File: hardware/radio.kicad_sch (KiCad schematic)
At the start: 5 parts

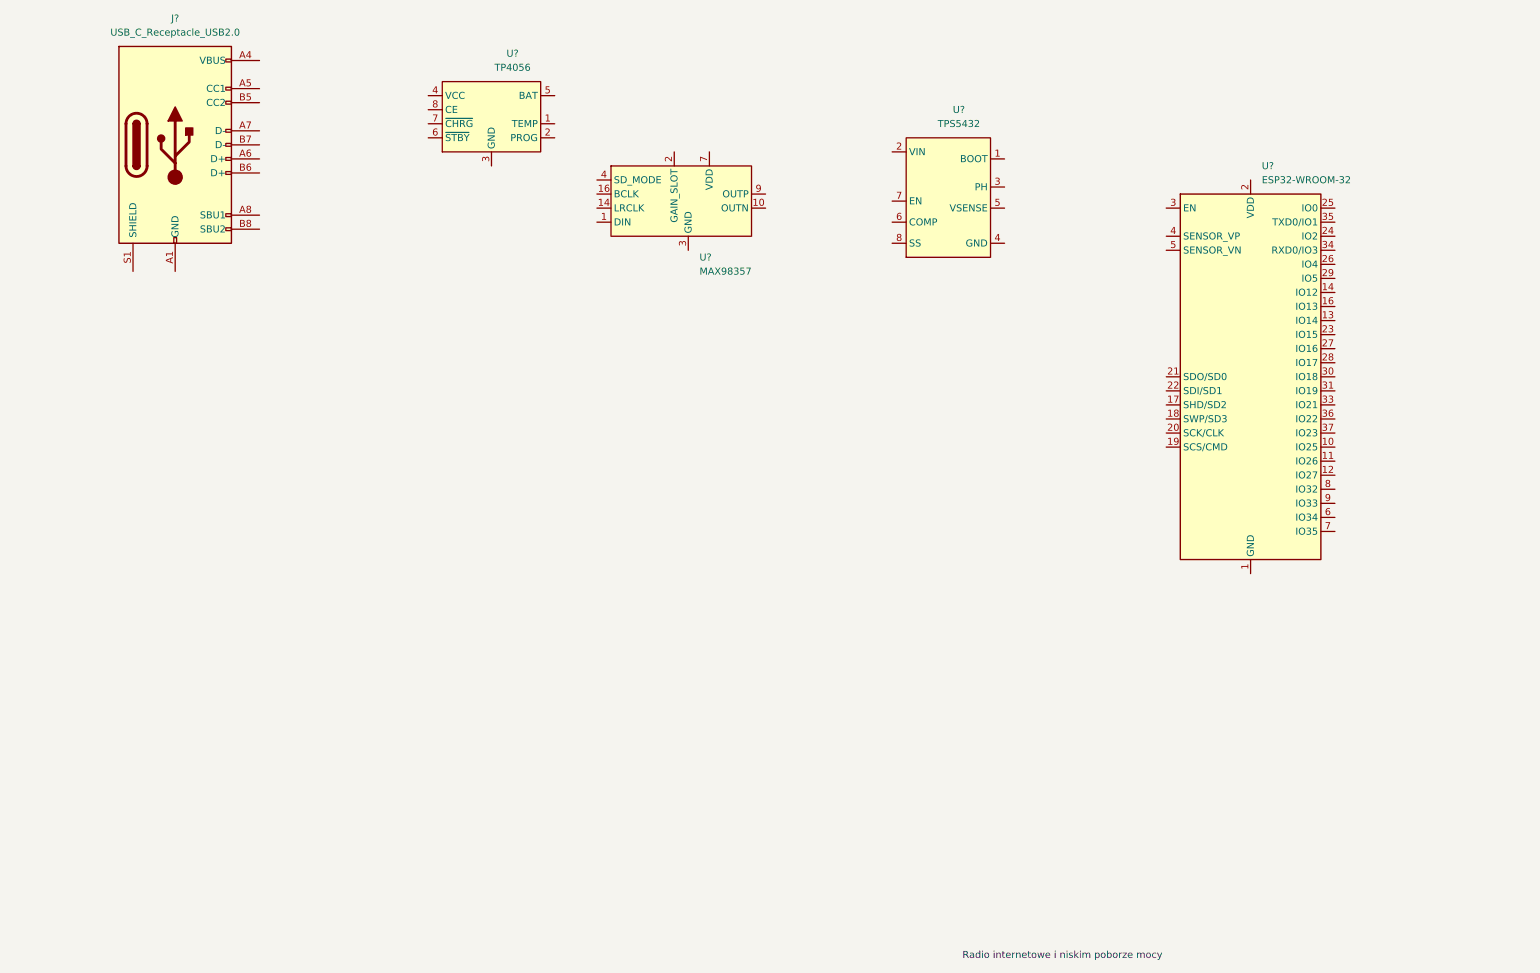
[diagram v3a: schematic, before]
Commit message: aktualizacja opisu symbolu OLED
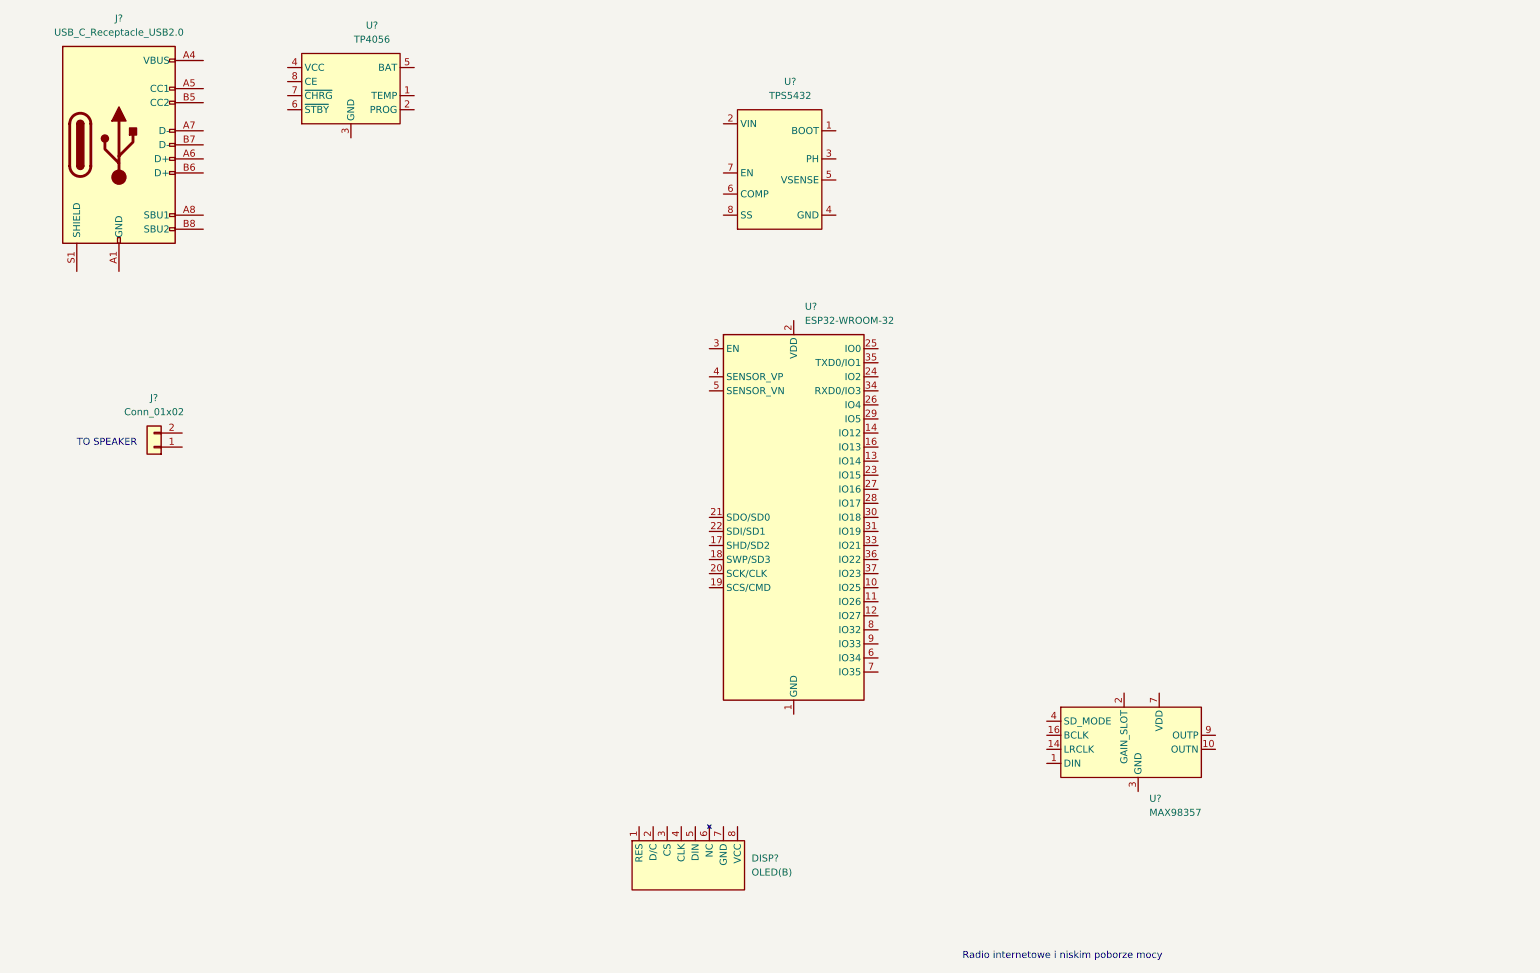
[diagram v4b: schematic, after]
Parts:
- added DISP?: OLED(B), symbol wyswietlacze:OLED(B)
- added J?: Conn_01x02, symbol Connector_Generic:Conn_01x02
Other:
- note added: "TO SPEAKER"
- moved on the sheet: J?, U?
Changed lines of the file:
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@@
     (effects (font (size 1.27 1.27)) (justify left bottom))
   )
-  (symbol (lib_id "scalaki:MAX98357") (at 138.43 53.34 0) (unit 1)
+  (text "TO SPEAKER\n" (at 27.94 97.79 0)
+    (effects (font (size 1.27 1.27)) (justify left bottom))
+  )
+  (symbol (lib_id "Connector_Generic:Conn_01x02") (at 41.91 97.79 180) (unit 1)
+    (in_bom no) (on_board yes) (fields_autoplaced)
+    (property "Reference" "J?" (id 0) (at 41.91 88.9 0))
+    (property "Value" "Conn_01x02" (id 1) (at 41.91 91.44 0))
+    (property "Footprint" "" (id 2) (at 41.91 97.79 0)
+      (effects (font (size 1.27 1.27)) hide)
+    )
+    (property "Datasheet" "~" (id 3) (at 41.91 97.79 0)
+      (effects (font (size 1.27 1.27)) hide)
+    )
+    (pin "1")
+    (pin "2")
+  )
+  (symbol (lib_id "scalaki:MAX98357") (at 219.71 151.13 0) (unit 1)
     (in_bom yes) (on_board yes) (fields_autoplaced)
-    (property "Reference" "U?" (id 0) (at 140.4494 63.5 0)
+    (property "Reference" "U?" (id 0) (at 221.7294 161.29 0)
       (effects (font (size 1.27 1.27)) (justify left))
     )
-    (property "Value" "MAX98357" (id 1) (at 140.4494 66.04 0)
+    (property "Value" "MAX98357" (id 1) (at 221.7294 163.83 0)
       (effects (font (size 1.27 1.27)) (justify left))
     )
-    (property "Footprint" "Package_DFN_QFN:TQFN-16-1EP_3x3mm_P0.5mm_EP1.23x1.23mm" (id 2) (at 138.43 53.34 0)
+    (property "Footprint" "Package_DFN_QFN:TQFN-16-1EP_3x3mm_P0.5mm_EP1.23x1.23mm" (id 2) (at 219.71 151.13 0)
       (effects (font (size 1.27 1.27)) hide)
     )
-    (property "Datasheet" "" (id 3) (at 138.43 53.34 0)
+    (property "Datasheet" "" (id 3) (at 219.71 151.13 0)
       (effects (font (size 1.27 1.27)) hide)
     )
@@
     (pin "9")
   )
-  (symbol (lib_id "RF_Module:ESP32-WROOM-32") (at 240.03 85.09 0) (unit 1)
+  (symbol (lib_id "RF_Module:ESP32-WROOM-32") (at 157.48 110.49 0) (unit 1)
     (in_bom yes) (on_board yes) (fields_autoplaced)
-    (property "Reference" "U?" (id 0) (at 242.0494 46.99 0)
+    (property "Reference" "U?" (id 0) (at 159.4994 72.39 0)
       (effects (font (size 1.27 1.27)) (justify left))
     )
-    (property "Value" "ESP32-WROOM-32" (id 1) (at 242.0494 49.53 0)
+    (property "Value" "ESP32-WROOM-32" (id 1) (at 159.4994 74.93 0)
       (effects (font (size 1.27 1.27)) (justify left))
     )
-    (property "Footprint" "RF_Module:ESP32-WROOM-32" (id 2) (at 240.03 123.19 0)
+    (property "Footprint" "RF_Module:ESP32-WROOM-32" (id 2) (at 157.48 148.59 0)
       (effects (font (size 1.27 1.27)) hide)
     )
-    (property "Datasheet" "https://www.espressif.com/sites/default/files/documentation/esp32-wroom-32_datasheet_en.pdf" (id 3) (at 232.41 83.82 0)
+    (property "Datasheet" "https://www.espressif.com/sites/default/files/documentation/esp32-wroom-32_datasheet_en.pdf" (id 3) (at 149.86 109.22 0)
       (effects (font (size 1.27 1.27)) hide)
     )
@@
     (pin "9")
   )
-  (symbol (lib_id "Connector:USB_C_Receptacle_USB2.0") (at 45.72 43.18 0) (unit 1)
+  (symbol (lib_id "Connector:USB_C_Receptacle_USB2.0") (at 35.56 43.18 0) (unit 1)
     (in_bom yes) (on_board yes) (fields_autoplaced)
-    (property "Reference" "J?" (id 0) (at 45.72 20.32 0))
-    (property "Value" "USB_C_Receptacle_USB2.0" (id 1) (at 45.72 22.86 0))
-    (property "Footprint" "" (id 2) (at 49.53 43.18 0)
+    (property "Reference" "J?" (id 0) (at 35.56 20.32 0))
+    (property "Value" "USB_C_Receptacle_USB2.0" (id 1) (at 35.56 22.86 0))
+    (property "Footprint" "" (id 2) (at 39.37 43.18 0)
       (effects (font (size 1.27 1.27)) hide)
     )
-    (property "Datasheet" "https://www.usb.org/sites/default/files/documents/usb_type-c.zip" (id 3) (at 49.53 43.18 0)
+    (property "Datasheet" "https://www.usb.org/sites/default/files/documents/usb_type-c.zip" (id 3) (at 39.37 43.18 0)
       (effects (font (size 1.27 1.27)) hide)
     )
@@
     (pin "S1")
   )
-  (symbol (lib_id "scalaki:TP4056") (at 102.87 38.1 0) (unit 1)
+  (symbol (lib_id "wyswietlacze:OLED(B)") (at 138.43 173.99 0) (unit 1)
     (in_bom yes) (on_board yes) (fields_autoplaced)
-    (property "Reference" "U?" (id 0) (at 106.68 26.67 0))
-    (property "Value" "TP4056" (id 1) (at 106.68 29.21 0))
-    (property "Footprint" "" (id 2) (at 100.33 39.37 0)
+    (property "Reference" "DISP?" (id 0) (at 149.86 172.0849 0)
+      (effects (font (size 1.27 1.27)) (justify left))
+    )
+    (property "Value" "OLED(B)" (id 1) (at 149.86 174.6249 0)
+      (effects (font (size 1.27 1.27)) (justify left))
+    )
+    (property "Footprint" "" (id 2) (at 146.05 179.07 0)
       (effects (font (size 1.27 1.27)) hide)
     )
-    (property "Datasheet" "" (id 3) (at 100.33 39.37 0)
+    (property "Datasheet" "" (id 3) (at 146.05 179.07 0)
+      (effects (font (size 1.27 1.27)) hide)
+    )
+    (pin "5")
+    (pin "6")
+    (pin "7")
+    (pin "8")
+    (pin "1")
+    (pin "2")
+    (pin "3")
+    (pin "4")
+  )
+  (symbol (lib_id "scalaki:TP4056") (at 77.47 33.02 0) (unit 1)
+    (in_bom yes) (on_board yes) (fields_autoplaced)
+    (property "Reference" "U?" (id 0) (at 81.28 21.59 0))
+    (property "Value" "TP4056" (id 1) (at 81.28 24.13 0))
+    (property "Footprint" "" (id 2) (at 74.93 34.29 0)
+      (effects (font (size 1.27 1.27)) hide)
+    )
+    (property "Datasheet" "" (id 3) (at 74.93 34.29 0)
       (effects (font (size 1.27 1.27)) hide)
     )
@@
     (pin "8")
   )
-  (symbol (lib_id "scalaki:TPS5432") (at 185.42 52.07 0) (unit 1)
+  (symbol (lib_id "scalaki:TPS5432") (at 154.94 46.99 0) (unit 1)
     (in_bom yes) (on_board yes) (fields_autoplaced)
-    (property "Reference" "U?" (id 0) (at 187.325 36.83 0))
-    (property "Value" "TPS5432" (id 1) (at 187.325 39.37 0))
-    (property "Footprint" "Package_SO:TI_SO-PowerPAD-8" (id 2) (at 193.04 64.77 0)
+    (property "Reference" "U?" (id 0) (at 156.845 31.75 0))
+    (property "Value" "TPS5432" (id 1) (at 156.845 34.29 0))
+    (property "Footprint" "Package_SO:TI_SO-PowerPAD-8" (id 2) (at 162.56 59.69 0)
       (effects (font (size 1.27 1.27)) hide)
     )
-    (property "Datasheet" "https://www.ti.com/lit/ds/slvsb89a/slvsb89a.pdf?ts=1654873515144&ref_url=https%253A%252F%252Fwww.google.com%252F" (id 3) (at 238.76 67.31 0)
+    (property "Datasheet" "https://www.ti.com/lit/ds/slvsb89a/slvsb89a.pdf?ts=1654873515144&ref_url=https%253A%252F%252Fwww.google.com%252F" (id 3) (at 208.28 62.23 0)
       (effects (font (size 1.27 1.27)) hide)
     )
@@
   )
   (symbol_instances
+    (path "/94ddeb71-8da5-4442-9ad2-5e3caa8f75f7"
+      (reference "DISP?") (unit 1) (value "OLED(B)") (footprint "")
+    )
+    (path "/3f9cf8a3-0501-4ef9-b5e0-7aea6a7eada3"
+      (reference "J?") (unit 1) (value "Conn_01x02") (footprint "")
+    )
     (path "/8b0ef56b-3e26-4f83-b202-0d062c709ccb"
       (reference "J?") (unit 1) (value "USB_C_Receptacle_USB2.0") (footprint "")

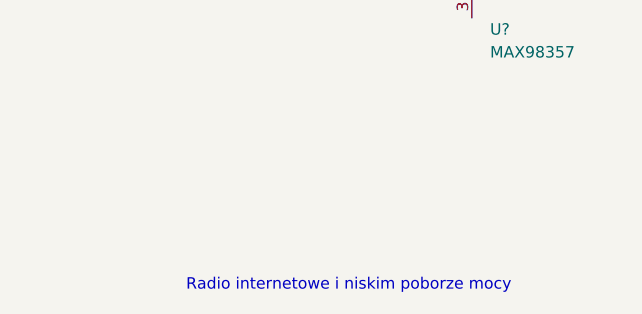
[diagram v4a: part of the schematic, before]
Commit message: przypisano footprint wyswietlacza do symbolu
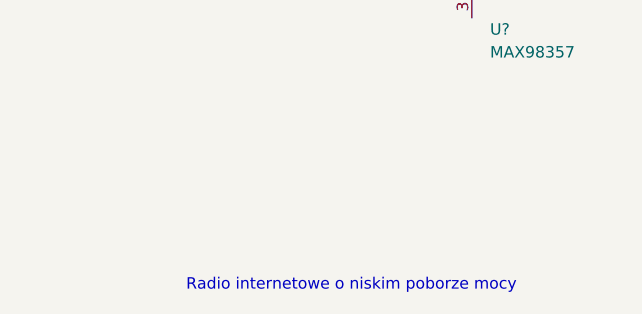
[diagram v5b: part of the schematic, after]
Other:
- note added: "Radio internetowe o niskim poborze mocy"
- note removed: "Radio internetowe i niskim poborze mocy"
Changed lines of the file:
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@@
 (kicad_sch (version 20211123) (generator eeschema)
   (paper "A4")
-  (text "Radio internetowe i niskim poborze mocy" (at 187.96 190.5 0)
+  (text "Radio internetowe o niskim poborze mocy" (at 187.96 190.5 0)
     (effects (font (size 1.27 1.27)) (justify left bottom))
   )

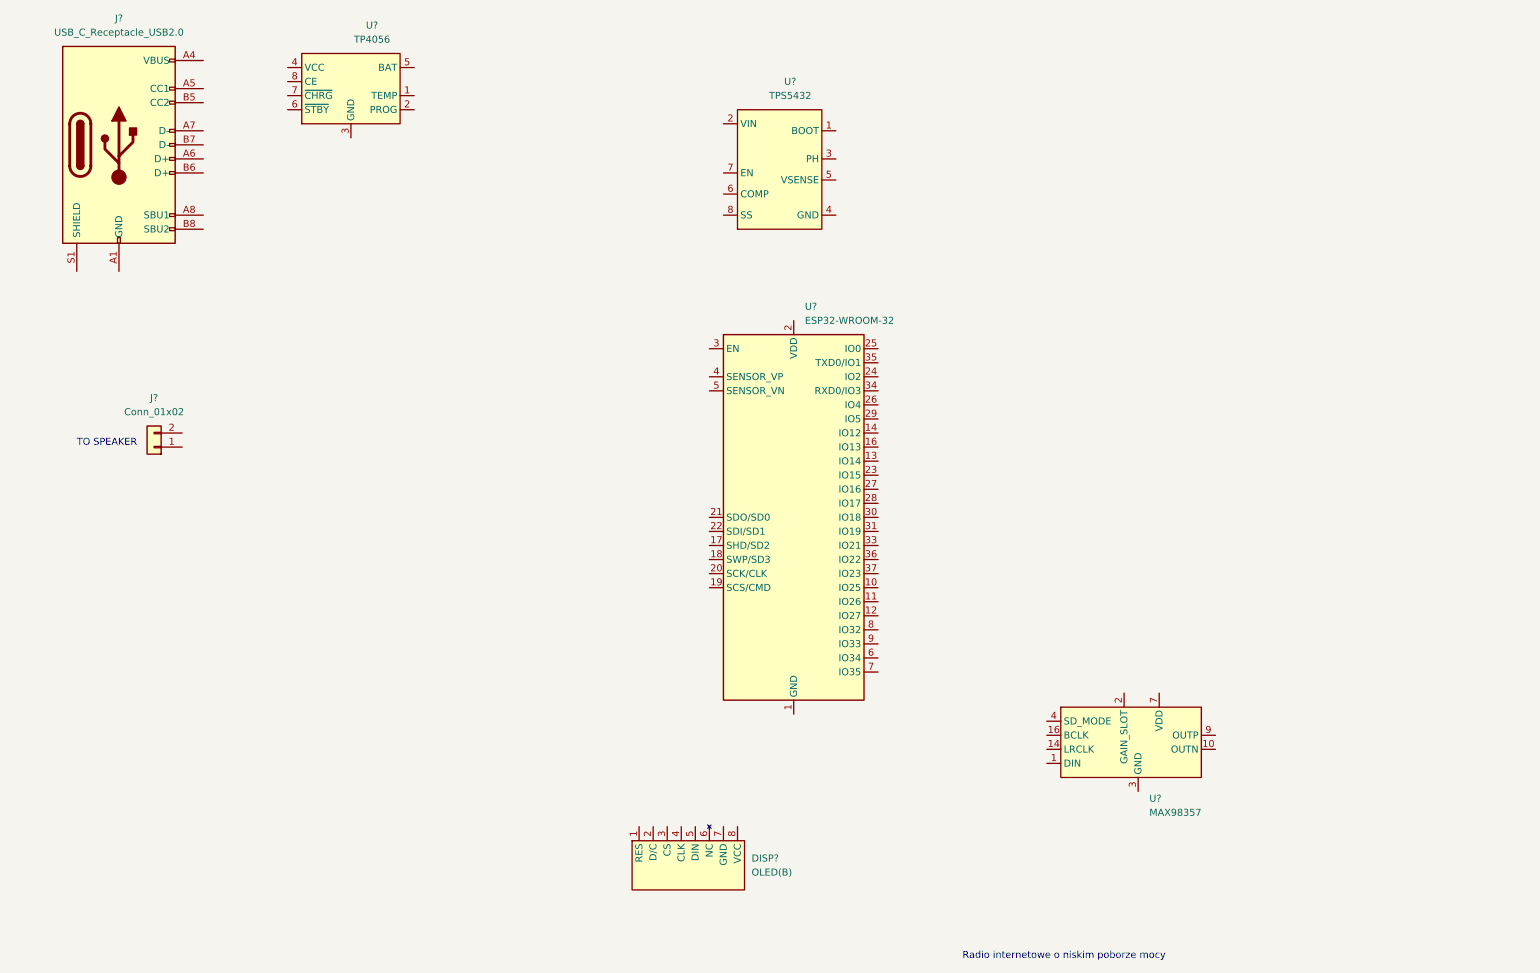
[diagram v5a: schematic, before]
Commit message: NETy zasilania i routing TP4056
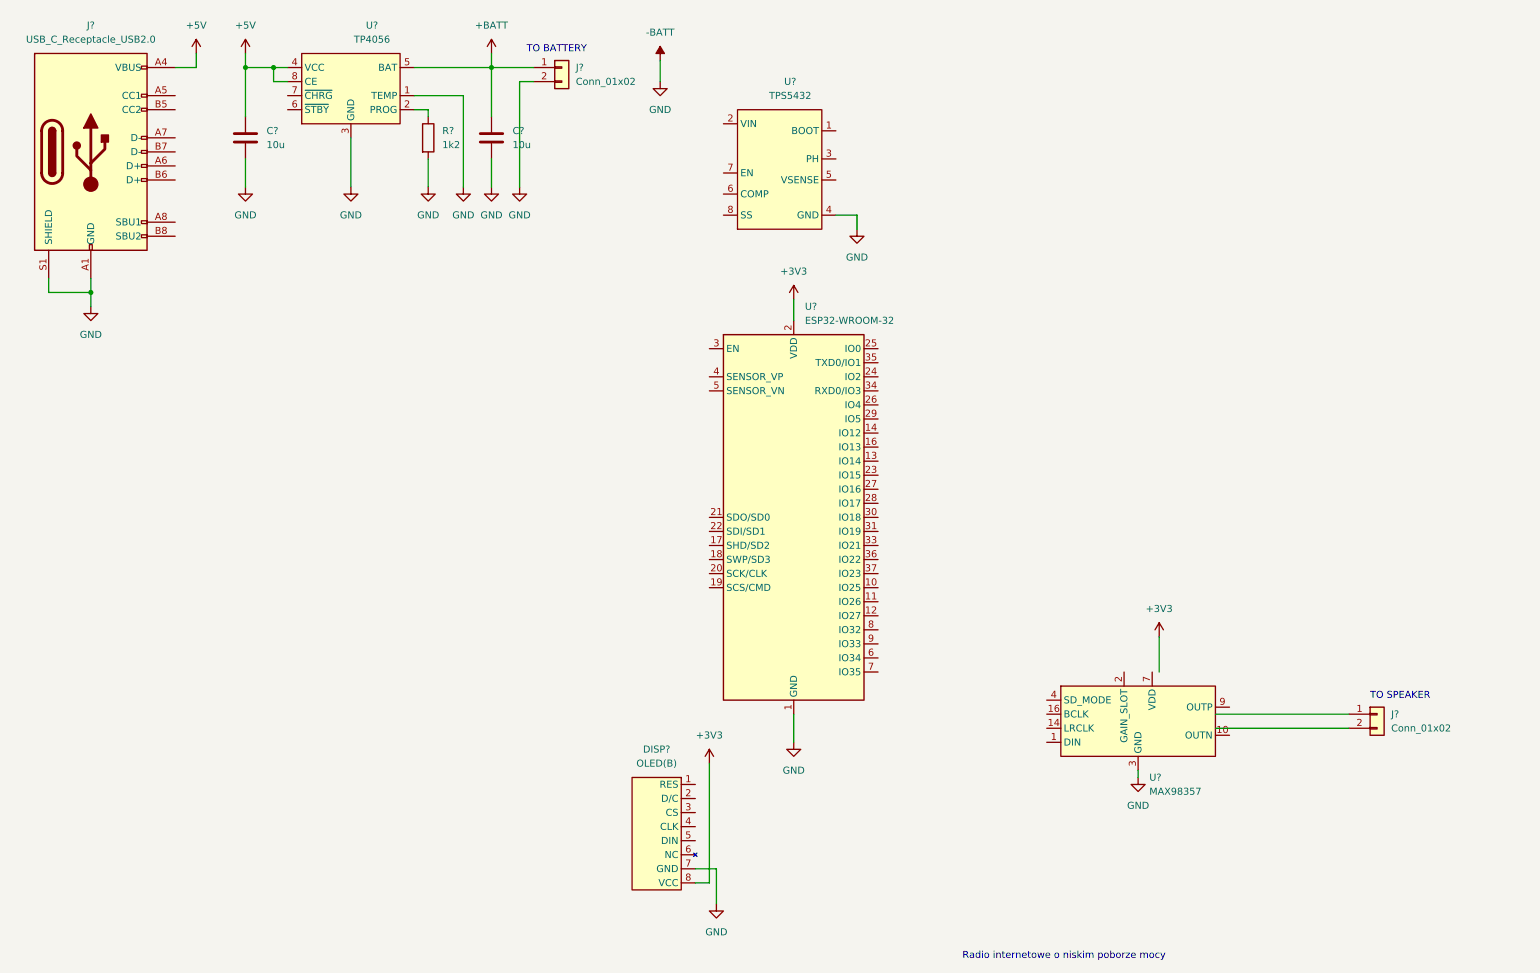
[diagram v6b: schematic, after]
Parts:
- added C? (x2): 10u, symbol Device:C
- added J?: Conn_01x02, symbol Connector_Generic:Conn_01x02
- added R?: 1k2, symbol Device:R
- DISP?: footprint (none) -> wyswietlacze:waveshare_oled
- U?: footprint (none) -> Package_SO:SOP-8-1EP_4.57x4.57mm_P1.27mm_EP4.57x4.45mm
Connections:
- net -BATT: now reaches U?.3 (GND)
- net -BATT: now also DISP?.7 (GND), J?.A1 (GND), J?.A12 (GND), J?.B1 (GND), J?.B12 (GND), J?.S1 (SHIELD), U?.1 (GND), U?.1 (TEMP), U?.15 (GND), U?.3 (GND), U?.38 (GND), U?.39 (GND), U?.4 (GND), C?.2, C?.2, J?.2 (Pin_2), R?.2
- net +3V3: now reaches U?.2 (VDD)
- net +3V3: now also DISP?.8 (VCC)
- net +5V: now reaches J?.A4 (VBUS), J?.A9 (VBUS), J?.B4 (VBUS), J?.B9 (VBUS)
- net +5V: now also U?.4 (VCC), U?.8 (CE), C?.1
- net at U?.2 (PROG): now also R?.1
- net +BATT: now reaches U?.5 (BAT)
- net +BATT: now also C?.1, J?.1 (Pin_1)
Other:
- note added: "TO BATTERY"
- moved on the sheet: DISP?, J?, U?

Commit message: schematic
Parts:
- added C? (x2): 10u, symbol Device:C
- added C? (x2): 22u, symbol Device:C
- added C? (x2): 100n, symbol Device:C
- added C?: 0.1u, symbol Device:C
- added C?: 10n, symbol Device:C
- added L?: 2.2u, symbol Device:L
- added R1: 47k, symbol Device:R
- added R2: 15k, symbol Device:R
- J?: now left out of the parts list
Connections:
- net +3V3: now also U?.7 (VDD), C?.1, C?.1, C?.2, C?.2, L?.2, R1.1
- net +BATT: now also U?.2 (VIN), C?.1, C?.1
- net -BATT: now also C?.1, C?.1, C?.1, C?.2, C?.2, C?.2, C?.2, C?.2, R2.2; no longer J?.S1 (SHIELD)
- net at J?.1 (Pin_1): now also U?.9 (OUTP)
- net at J?.2 (Pin_2): now also U?.10 (OUTN)
- net at U?.1 (BOOT): now also C?.2
- net at U?.3 (PH): now also L?.1
- net at U?.5 (VSENSE): now also R1.2, R2.1
- net at U?.8 (SS): now also C?.1
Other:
- note added: "EN has internal pull-up"
- note added: "For 3,3V R2/R1 = 0,3232"
- note added: "Pull to ground to disable converter"
- note added: "Recommended to start with 10k for R1, increase for lower currents"
- moved on the sheet: DISP?, J?, U?
